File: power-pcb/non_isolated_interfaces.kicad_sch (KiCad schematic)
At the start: 62 parts, among them J1 Network Connector, J2 Screw_Terminal_01x02, J3 STDC14, J4 USB_C_Receptacle_USB2.0_16P, U1 TPS5430DDA, U3 ECMF02-2AMX6, U4 AMS1117-3.3, U5 SN65HVD230

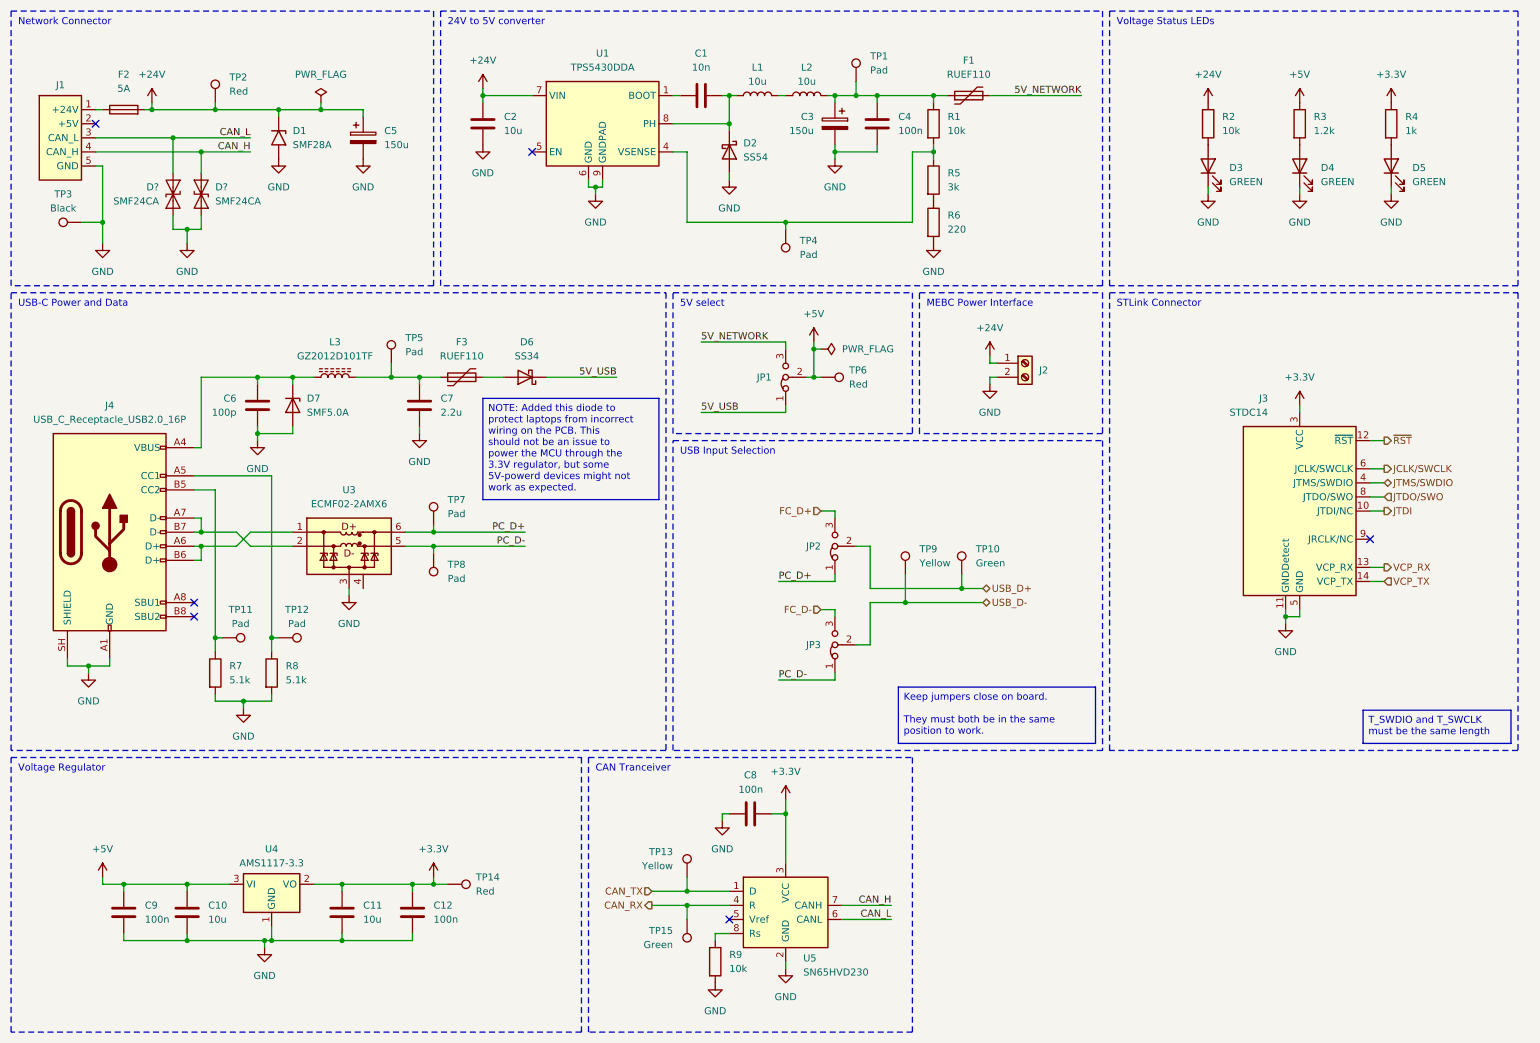
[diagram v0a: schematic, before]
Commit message: power-pcb: re-annotate schematic and start board
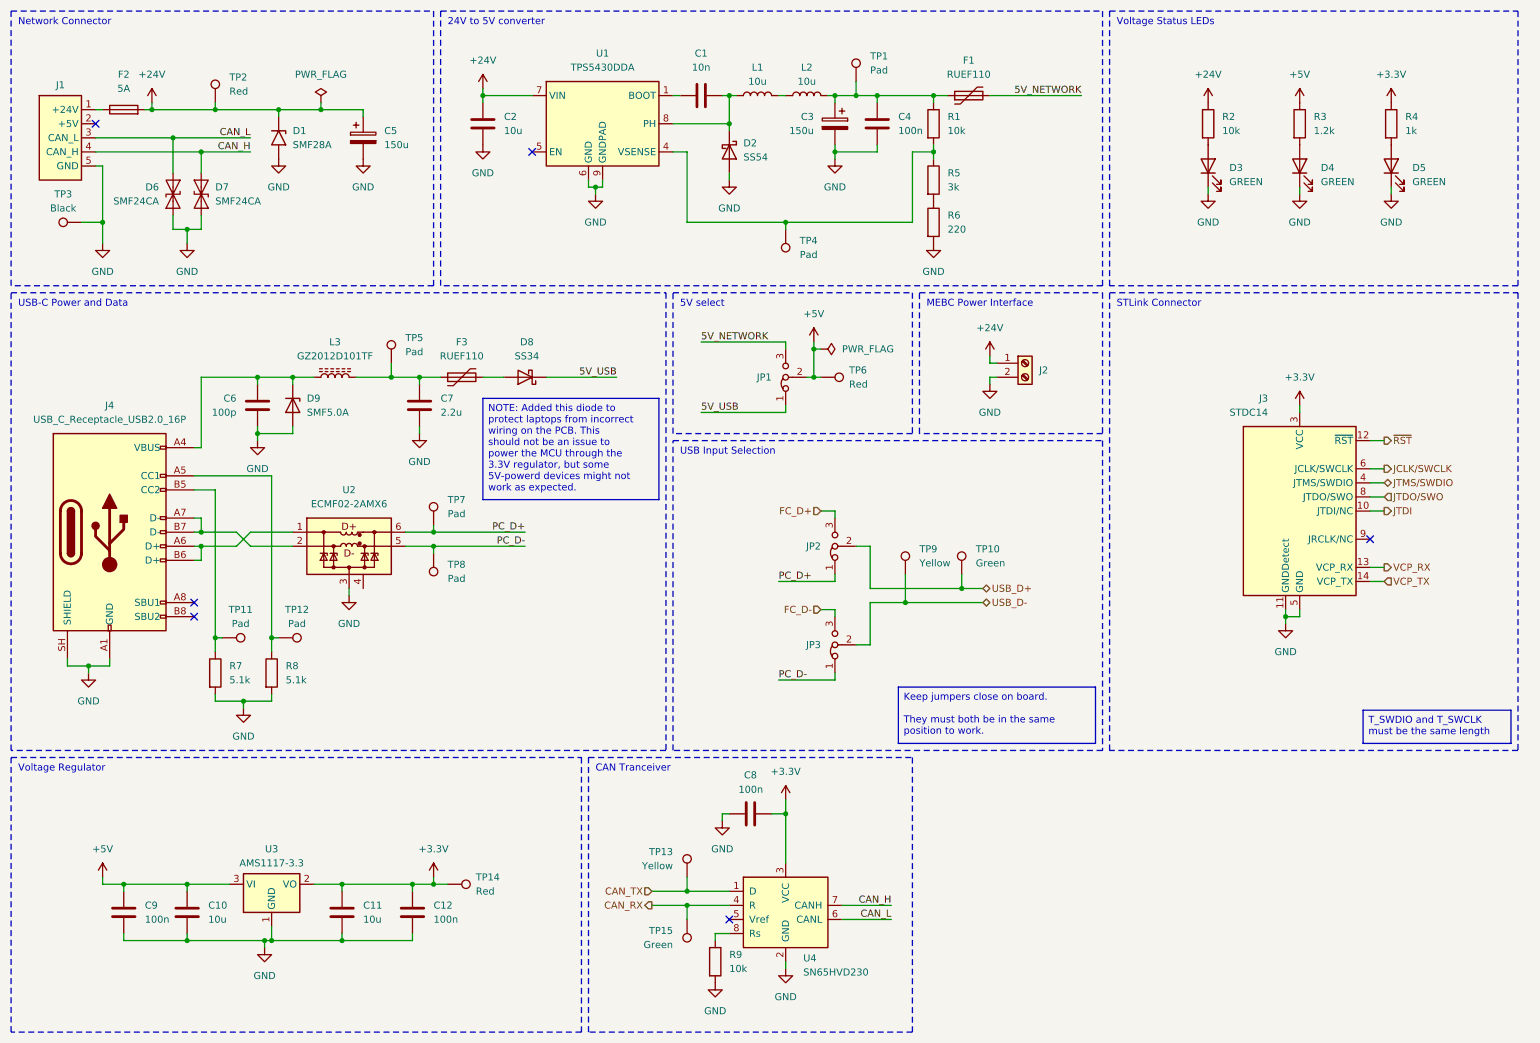
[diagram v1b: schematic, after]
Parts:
- gave numbers to parts that had none: 2
- renumbered D6 to D8, D7 to D9, U3 to U2, U4 to U3, U5 to U4
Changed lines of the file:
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@@
 		(dnp no)
 		(fields_autoplaced yes)
-		(property "Reference" "U4"
+		(property "Reference" "U3"
 			(at 59.69 163.83 0)
 			(show_name no)
@@
 			(project "power-pcb"
 				(path "/4b4cf3aa-c94c-4150-b9c5-35049cd71136/d2b1a814-a8ab-491d-a39f-63fa9799b0cb"
-					(reference "U4")
+					(reference "U3")
 					(unit 1)
 					(variant
@@
 		(dnp no)
 		(fields_autoplaced yes)
-		(property "Reference" "U3"
+		(property "Reference" "U2"
 			(at 73.66 99.06 0)
 			(show_name no)
@@
 			(project "power-pcb"
 				(path "/4b4cf3aa-c94c-4150-b9c5-35049cd71136/d2b1a814-a8ab-491d-a39f-63fa9799b0cb"
-					(reference "U3")
+					(reference "U2")
 					(unit 1)
 					(variant
@@
 		(dnp no)
 		(fields_autoplaced yes)
-		(property "Reference" "D6"
+		(property "Reference" "D8"
 			(at 105.7275 72.39 0)
 			(show_name no)
@@
 			(project "power-pcb"
 				(path "/4b4cf3aa-c94c-4150-b9c5-35049cd71136/d2b1a814-a8ab-491d-a39f-63fa9799b0cb"
-					(reference "D6")
+					(reference "D8")
 					(unit 1)
 					(variant
@@
 		(in_pos_files yes)
 		(dnp no)
-		(property "Reference" "D?"
+		(property "Reference" "D6"
 			(at 39.37 44.4499 90)
 			(show_name no)
@@
 			(project "power-pcb"
 				(path "/4b4cf3aa-c94c-4150-b9c5-35049cd71136/d2b1a814-a8ab-491d-a39f-63fa9799b0cb"
-					(reference "D?")
+					(reference "D6")
 					(unit 1)
 					(variant
@@
 		(dnp no)
 		(fields_autoplaced yes)
-		(property "Reference" "#PWR013"
+		(property "Reference" "#PWR012"
 			(at 76.2 45.72 0)
 			(hide yes)
@@
 			(project "power-pcb"
 				(path "/4b4cf3aa-c94c-4150-b9c5-35049cd71136/d2b1a814-a8ab-491d-a39f-63fa9799b0cb"
-					(reference "#PWR013")
+					(reference "#PWR012")
 					(unit 1)
 				)
@@
 		(in_pos_files yes)
 		(dnp no)
-		(property "Reference" "U5"
+		(property "Reference" "U4"
 			(at 155.575 183.515 0)
 			(show_name no)
@@
 			(project "power-pcb"
 				(path "/4b4cf3aa-c94c-4150-b9c5-35049cd71136/d2b1a814-a8ab-491d-a39f-63fa9799b0cb"
-					(reference "U5")
+					(reference "U4")
 					(unit 1)
 					(variant
@@
 		(dnp no)
 		(fields_autoplaced yes)
-		(property "Reference" "#PWR012"
+		(property "Reference" "#PWR011"
 			(at 60.96 45.72 0)
 			(hide yes)
@@
 			(project "power-pcb"
 				(path "/4b4cf3aa-c94c-4150-b9c5-35049cd71136/d2b1a814-a8ab-491d-a39f-63fa9799b0cb"
-					(reference "#PWR012")
+					(reference "#PWR011")
 					(unit 1)
 				)
@@
 		(dnp no)
 		(fields_autoplaced yes)
-		(property "Reference" "#PWR011"
+		(property "Reference" "#PWR013"
 			(at 161.29 45.72 0)
 			(hide yes)
@@
 			(project "power-pcb"
 				(path "/4b4cf3aa-c94c-4150-b9c5-35049cd71136/d2b1a814-a8ab-491d-a39f-63fa9799b0cb"
-					(reference "#PWR011")
+					(reference "#PWR013")
 					(unit 1)
 				)
@@
 		(dnp no)
 		(fields_autoplaced yes)
-		(property "Reference" "D?"
+		(property "Reference" "D7"
 			(at 49.53 44.4499 90)
 			(show_name no)
@@
 			(project "power-pcb"
 				(path "/4b4cf3aa-c94c-4150-b9c5-35049cd71136/d2b1a814-a8ab-491d-a39f-63fa9799b0cb"
-					(reference "D?")
+					(reference "D7")
 					(unit 1)
 					(variant
@@
 		(dnp no)
 		(fields_autoplaced yes)
-		(property "Reference" "D7"
+		(property "Reference" "D9"
 			(at 66.04 82.5499 90)
 			(show_name no)
@@
 			(project "power-pcb"
 				(path "/4b4cf3aa-c94c-4150-b9c5-35049cd71136/d2b1a814-a8ab-491d-a39f-63fa9799b0cb"
-					(reference "D7")
+					(reference "D9")
 					(unit 1)
 					(variant

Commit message: power-pcb: fix schematic after review
- Add footprint for resitive load for the RECOM
- Add Opamps when useful
- Add capacitor and change some footprint sizes
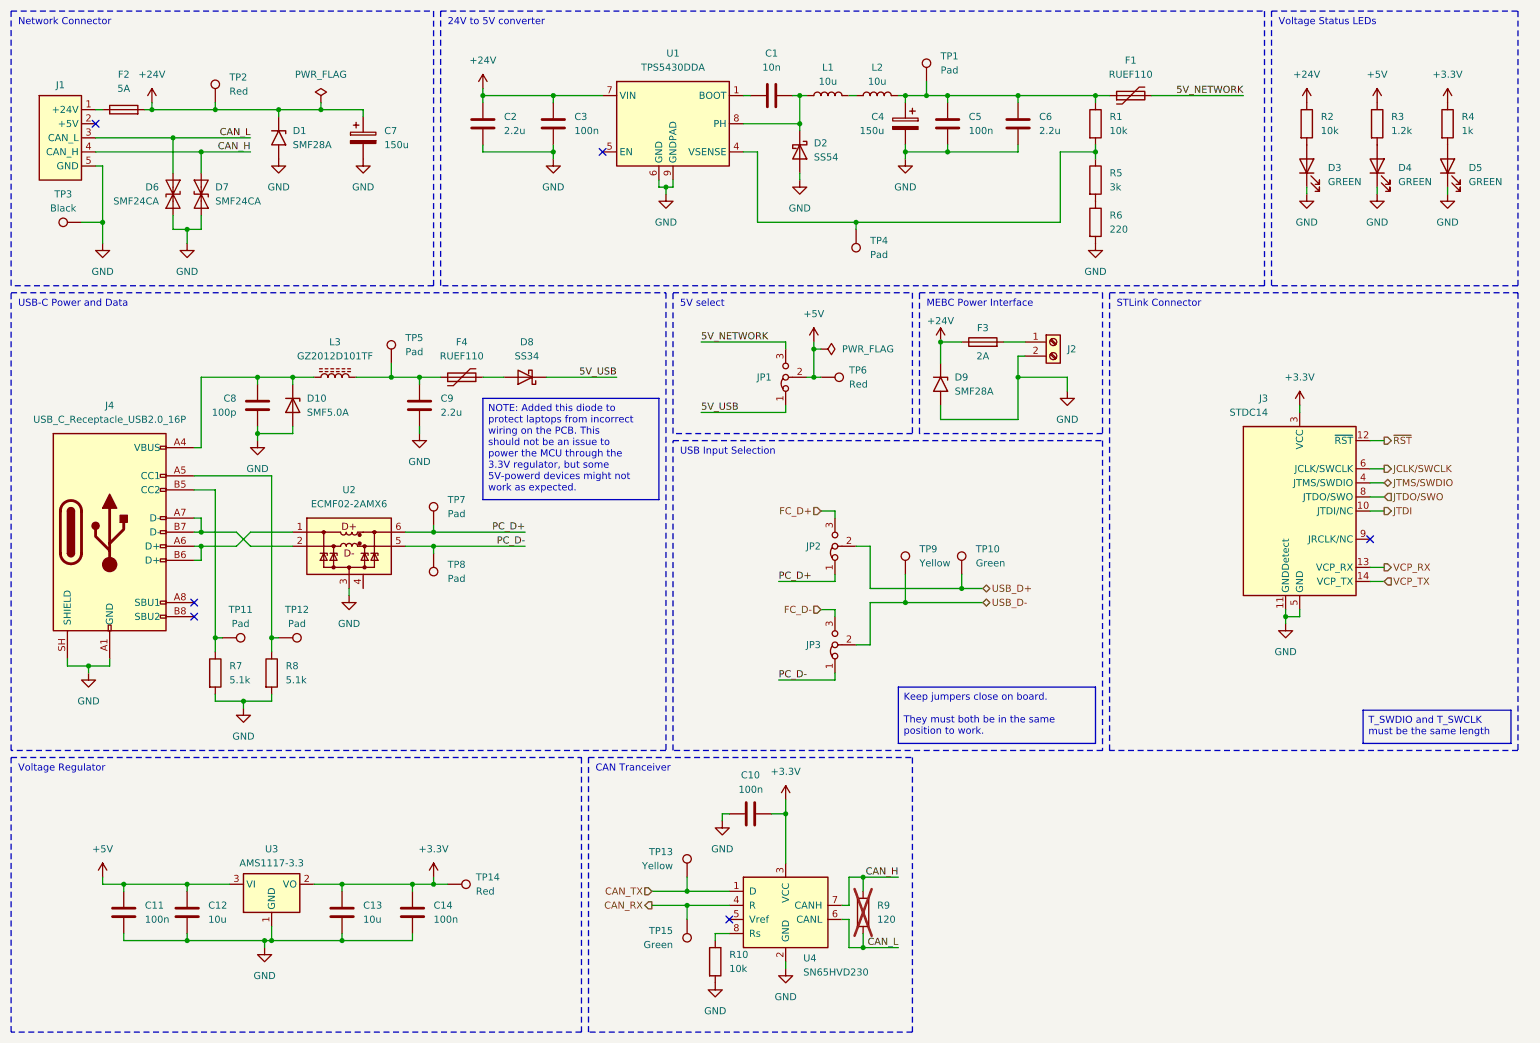
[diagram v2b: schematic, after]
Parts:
- added C3: 100n, Capacitor_SMD:C_0402_1005Metric_Pad0.74x0.62mm_HandSolder, symbol Device:C
- added C6: 2.2u, Capacitor_SMD:C_0805_2012Metric_Pad1.18x1.45mm_HandSolder, symbol Device:C
- added D9: SMF28A, Diode_SMD:D_SMF, symbol Diode:SMF28A
- added F3: 2A, Exocet:Fuseholder_Littelfuse_Combined, symbol Device:Fuse
- added R9: 120, Resistor_THT:R_Axial_DIN0309_L9.0mm_D3.2mm_P12.70mm_Horizontal, symbol Device:R
- C10: renamed from C8; footprint Capacitor_SMD:C_0603_1608Metric_Pad1.08x0.95mm_HandSolder -> Capacitor_SMD:C_0402_1005Metric_Pad0.74x0.62mm_HandSolder; JLCPCB C14663 -> C307331
- C11: renamed from C9; footprint Capacitor_SMD:C_0603_1608Metric_Pad1.08x0.95mm_HandSolder -> Capacitor_SMD:C_0402_1005Metric_Pad0.74x0.62mm_HandSolder; JLCPCB C14663 -> C307331
- C14: renamed from C12; footprint Capacitor_SMD:C_0603_1608Metric_Pad1.08x0.95mm_HandSolder -> Capacitor_SMD:C_0402_1005Metric_Pad0.74x0.62mm_HandSolder; JLCPCB C14663 -> C307331
- C2: value 10u -> 2.2u; footprint Capacitor_SMD:C_1206_3216Metric_Pad1.33x1.80mm_HandSolder -> Capacitor_SMD:C_0805_2012Metric_Pad1.18x1.45mm_HandSolder; JLCPCB C13585 -> C377773
- C5: renamed from C4; footprint Capacitor_SMD:C_0603_1608Metric_Pad1.08x0.95mm_HandSolder -> Capacitor_SMD:C_0402_1005Metric_Pad0.74x0.62mm_HandSolder; JLCPCB C14663 -> C307331
- renumbered C10 to C12, C11 to C13, C3 to C4, C5 to C7, C6 to C8, C7 to C9, D9 to D10, F3 to F4, R9 to R10
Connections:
- net +24V: now also C2.2, C3.1, D9.1 (A1), F3.1; no longer C2.1, J2.1 (Pin_1)
- net CAN_H: now also R9.1
- net CAN_L: now also R9.2
- net GND: now also C2.1, C3.2, C6.1, D9.2 (A2); no longer C2.2
- net at C4.1, C5.1, F1.1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: now also C6.2
- new net: F3.2, J2.1 (Pin_1)
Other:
- moved on the sheet: C1, C4, C5, D2, D3, D4, D5, F1, J2, L1, L2, R1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

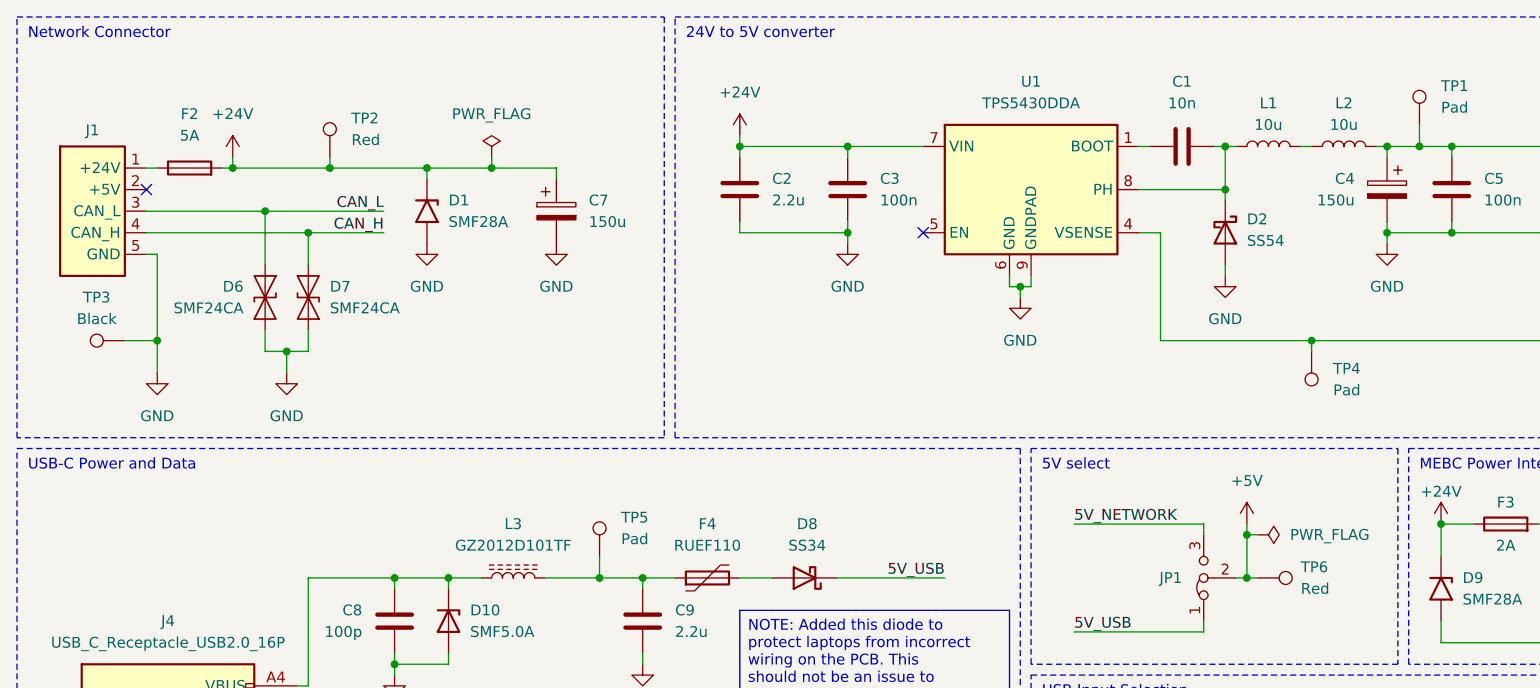
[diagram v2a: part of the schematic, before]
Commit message: power-pcb: work on part placement and JLCPCB DNP
Some of the components that were recentlt added had not been marked as
DNP for JLCPCB yet, this is now done.
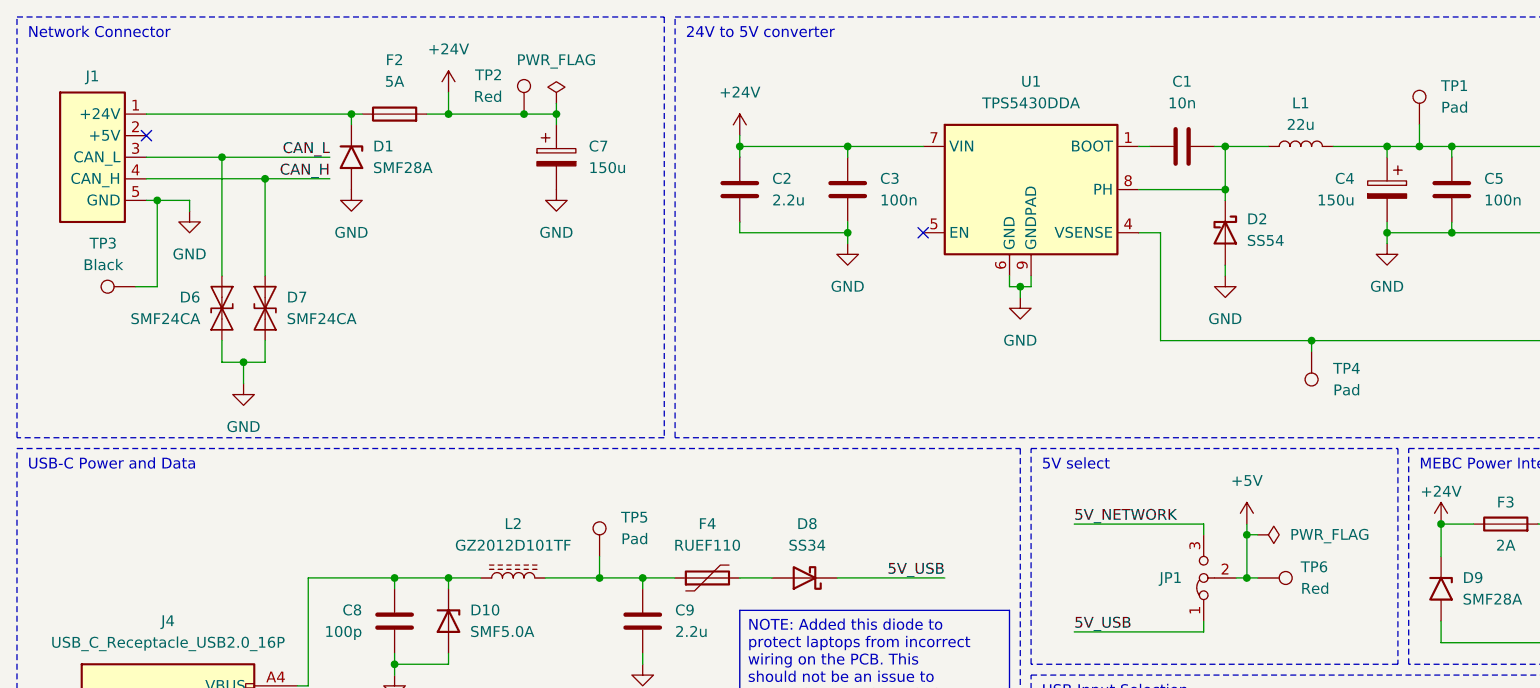
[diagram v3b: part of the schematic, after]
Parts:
- removed L2: 10u, Inductor_THT:L_Radial_D8.7mm_P5.00mm_Fastron_07HCP, symbol Device:L
- C4: footprint Capacitor_THT:CP_Radial_D5.0mm_P2.00mm -> Capacitor_THT:CP_Radial_D8.0mm_P3.50mm; MPN 860020272007 -> 860020574010
- C7: footprint Capacitor_THT:CP_Radial_D5.0mm_P2.00mm -> Capacitor_THT:CP_Radial_D8.0mm_P3.50mm; DIST -- mixed values -- -> (none); MPN 860020272007 -> 860020574010; Part Name -- mixed values -- -> (none)
- L1: value 10u -> 22u; footprint Inductor_THT:L_Radial_D8.7mm_P5.00mm_Fastron_07HCP -> Inductor_THT:L_Axial_L16.0mm_D6.3mm_P5.08mm_Vertical_Fastron_VHBCC; MFR Bourns Inc. -> Abracon LLC; MPN RLB0914-100KL -> AIAP-02-220K
- renumbered L3 to L2
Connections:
- net +24V: no longer D1.1 (A1)
- net at C4.1, C5.1, C6.2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: now also L1.2
- net at F2.1, J1.1 (+24V): now also D1.1 (A1)
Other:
- moved on the sheet: C7, D1, D6, D7, F2, J1, TP2, TP3
